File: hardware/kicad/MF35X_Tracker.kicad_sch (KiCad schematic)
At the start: 14 parts, among them J1 External GPIO11 logic output, J2 5V power input from DC/DC, J3 VDO oil-temp NTC - return/cas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, J4 Oil-pressure sender - return/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, J5 Vehicle battery sense input, U1 Freenove ESP32-S3 WROOM Lite 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, U2 ADS1115 @ 0x48, U3 GPS module - VCC TBD, U4 MAX31855 K-type - VCC TBD, U5 HY-M154 / PC817 RPM interface

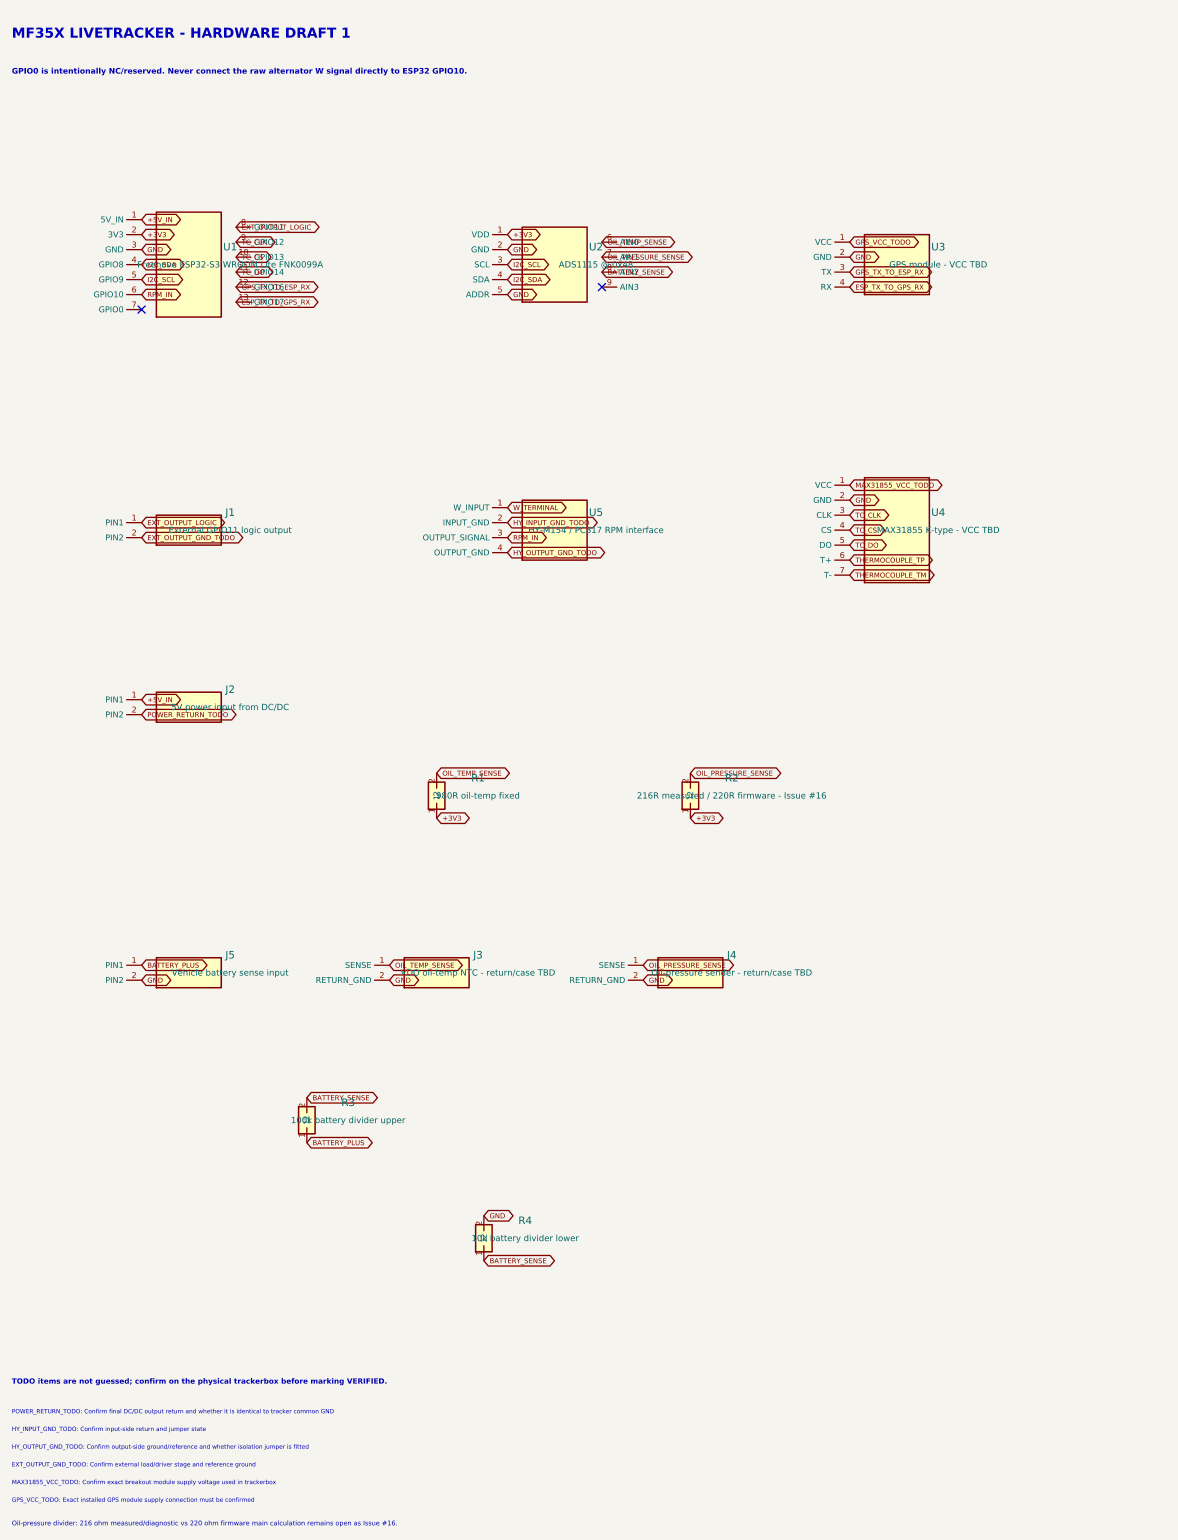
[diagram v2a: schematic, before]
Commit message: Regenerate confirmed trackerbox wiring
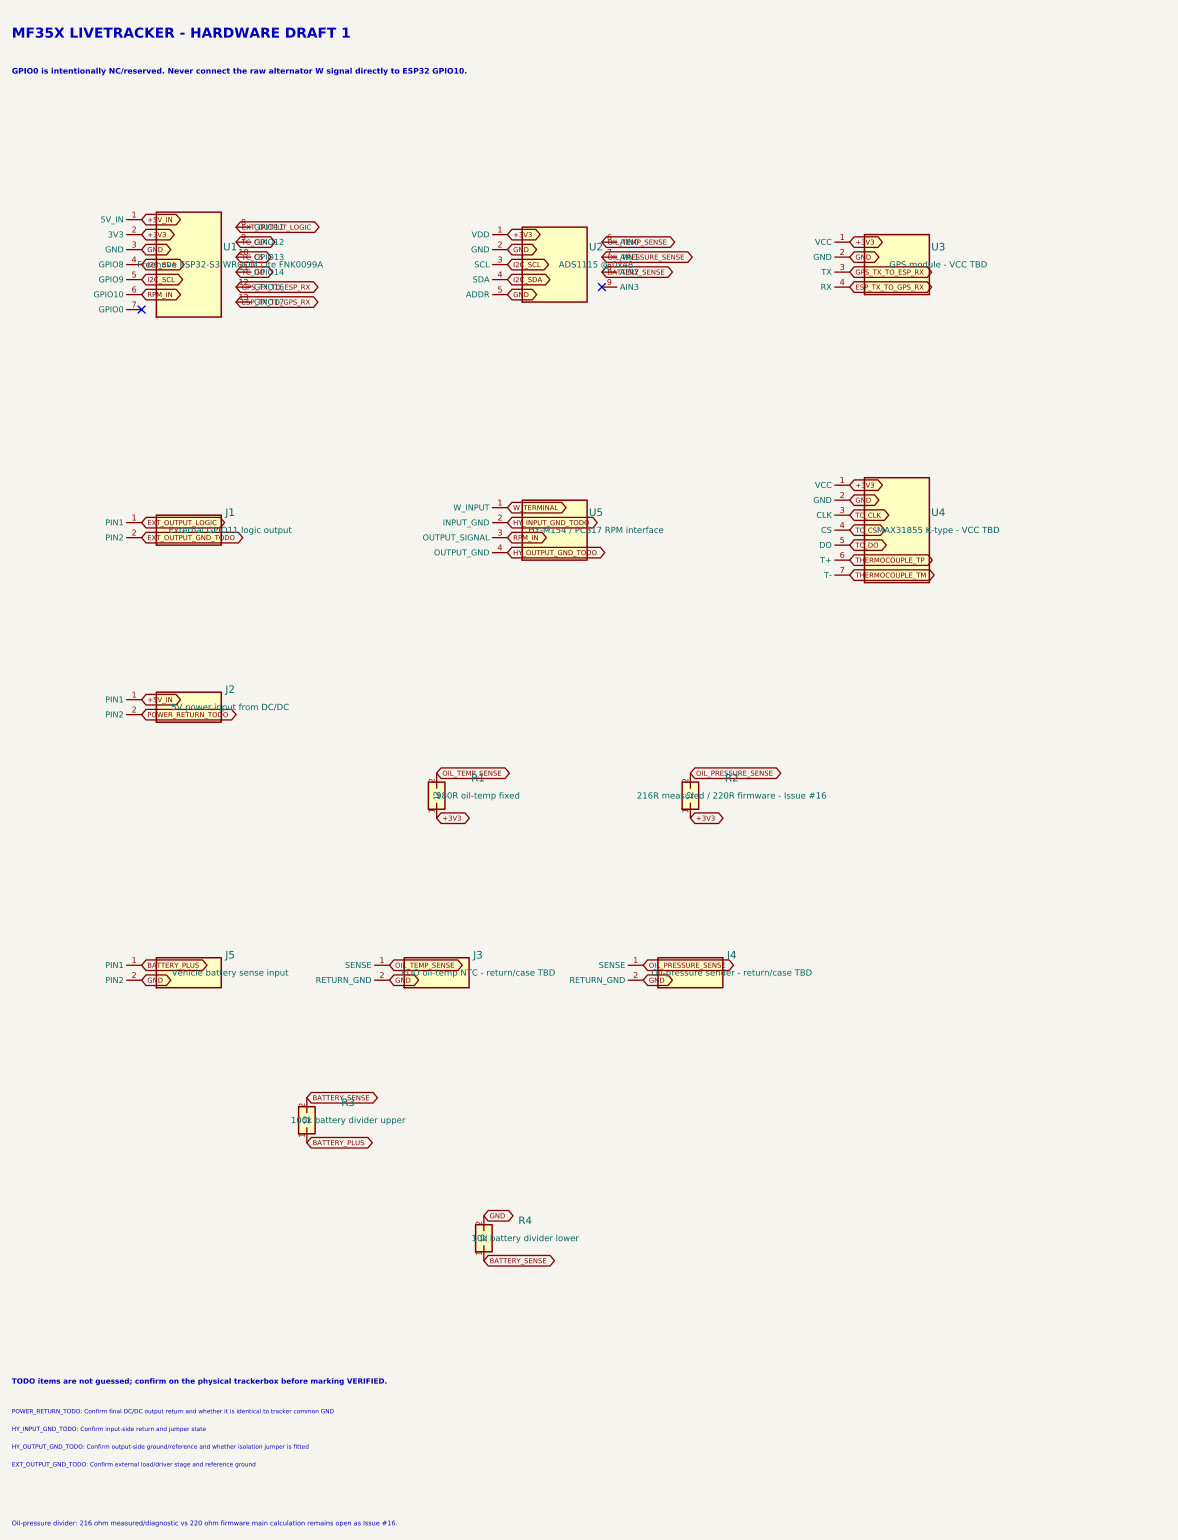
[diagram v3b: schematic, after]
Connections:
- net GPS_VCC_TODO is gone; now on net +3V3: U3.1 (VCC)
- net MAX31855_VCC_TODO is gone; now on net +3V3: U4.1 (VCC)
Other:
- note removed: "GPS_VCC_TODO: Exact installed GPS module supply connection must be confirmed"
- note removed: "MAX31855_VCC_TODO: Confirm exact breakout module supply voltage used in trackerbox"
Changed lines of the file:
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@@
     (effects (font (size 0.85 0.85)) (justify left))
   )
-  (global_label "GPS_VCC_TODO" (shape bidirectional) (at 162.00 51.19 0)
+  (global_label "+3V3" (shape bidirectional) (at 162.00 51.19 0)
     (effects (font (size 0.85 0.85)) (justify left))
   )
@@
     (effects (font (size 0.85 0.85)) (justify left))
   )
-  (global_label "MAX31855_VCC_TODO" (shape bidirectional) (at 162.00 92.38 0)
+  (global_label "+3V3" (shape bidirectional) (at 162.00 92.38 0)
     (effects (font (size 0.85 0.85)) (justify left))
   )
@@
     (effects (font (size 0.72 0.72)) (justify left bottom))
   )
-  (text "MAX31855_VCC_TODO: Confirm exact breakout module supply voltage used in trackerbox" (at 20.00 262.00 0)
-    (effects (font (size 0.72 0.72)) (justify left bottom))
-  )
-  (text "GPS_VCC_TODO: Exact installed GPS module supply connection must be confirmed" (at 20.00 265.00 0)
-    (effects (font (size 0.72 0.72)) (justify left bottom))
-  )

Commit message: Regenerate HY-M154 and solenoid wiring
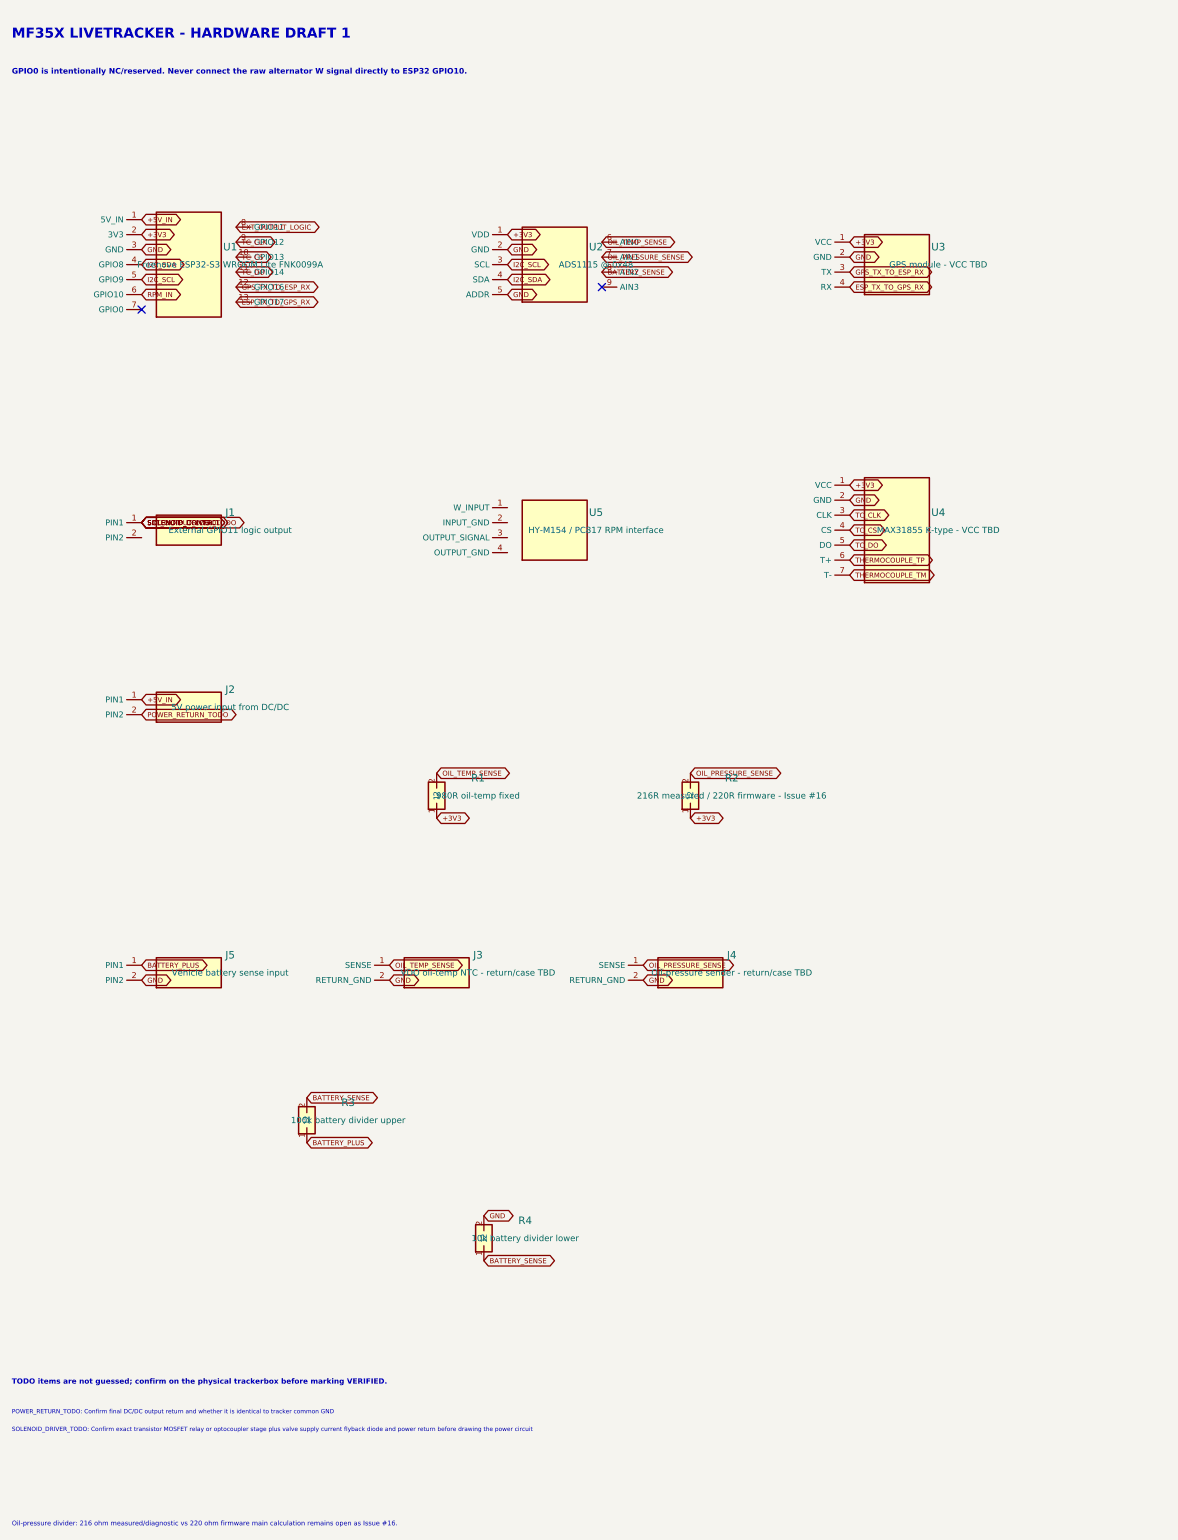
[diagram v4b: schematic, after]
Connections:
- net RPM_IN: no longer U5.3 (OUTPUT_SIGNAL)
- net EXT_OUTPUT_GND_TODO: no longer names the net of J1.2 (PIN2)
- net HY_INPUT_GND_TODO: no longer names the net of U5.2 (INPUT_GND)
- net HY_OUTPUT_GND_TODO: no longer names the net of U5.4 (OUTPUT_GND)
- net W_TERMINAL: no longer names the net of U5.1 (W_INPUT)
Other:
- note added: "SOLENOID_DRIVER_TODO: Confirm exact transistor MOSFET relay or optocoupler stage plus valve supply current flyback diode and power return before drawing the power circuit"
- note removed: "EXT_OUTPUT_GND_TODO: Confirm external load/driver stage and reference ground"
- note removed: "HY_INPUT_GND_TODO: Confirm input-side return and jumper state"
- note removed: "HY_OUTPUT_GND_TODO: Confirm output-side ground/reference and whether isolation jumper is fitted"
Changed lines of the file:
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@@
     (effects (font (size 0.85 0.85)) (justify left))
   )
-  (global_label "EXT_OUTPUT_GND_TODO" (shape bidirectional) (at 42.00 101.27 0)
+  (global_label "SOLENOID_CONTROL" (shape bidirectional) (at 42.00 98.73 0)
+    (effects (font (size 0.85 0.85)) (justify left))
+  )
+  (global_label "SOLENOID_DRIVER_TODO" (shape bidirectional) (at 42.00 98.73 0)
     (effects (font (size 0.85 0.85)) (justify left))
   )
@@
     (effects (font (size 0.85 0.85)) (justify left))
   )
-  (global_label "HY_INPUT_GND_TODO" (shape bidirectional) (at 104.00 98.73 0)
-    (effects (font (size 0.85 0.85)) (justify left))
-  )
-  (global_label "HY_OUTPUT_GND_TODO" (shape bidirectional) (at 104.00 103.81 0)
-    (effects (font (size 0.85 0.85)) (justify left))
-  )
-  (global_label "RPM_IN" (shape bidirectional) (at 104.00 101.27 0)
-    (effects (font (size 0.85 0.85)) (justify left))
-  )
-  (global_label "W_TERMINAL" (shape bidirectional) (at 104.00 96.19 0)
-    (effects (font (size 0.85 0.85)) (justify left))
-  )
   (no_connect (at 42.00 62.62))
   (no_connect (at 120.00 58.81))
@@
     (effects (font (size 0.72 0.72)) (justify left bottom))
   )
-  (text "HY_INPUT_GND_TODO: Confirm input-side return and jumper state" (at 20.00 253.00 0)
+  (text "SOLENOID_DRIVER_TODO: Confirm exact transistor MOSFET relay or optocoupler stage plus valve supply current flyback diode and power return before drawing the power circuit" (at 20.00 253.00 0)
     (effects (font (size 0.72 0.72)) (justify left bottom))
   )
-  (text "HY_OUTPUT_GND_TODO: Confirm output-side ground/reference and whether isolation jumper is fitted" (at 20.00 256.00 0)
-    (effects (font (size 0.72 0.72)) (justify left bottom))
-  )
-  (text "EXT_OUTPUT_GND_TODO: Confirm external load/driver stage and reference ground" (at 20.00 259.00 0)
-    (effects (font (size 0.72 0.72)) (justify left bottom))
-  )

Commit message: Generate KiCad trackerbox HW-REV1
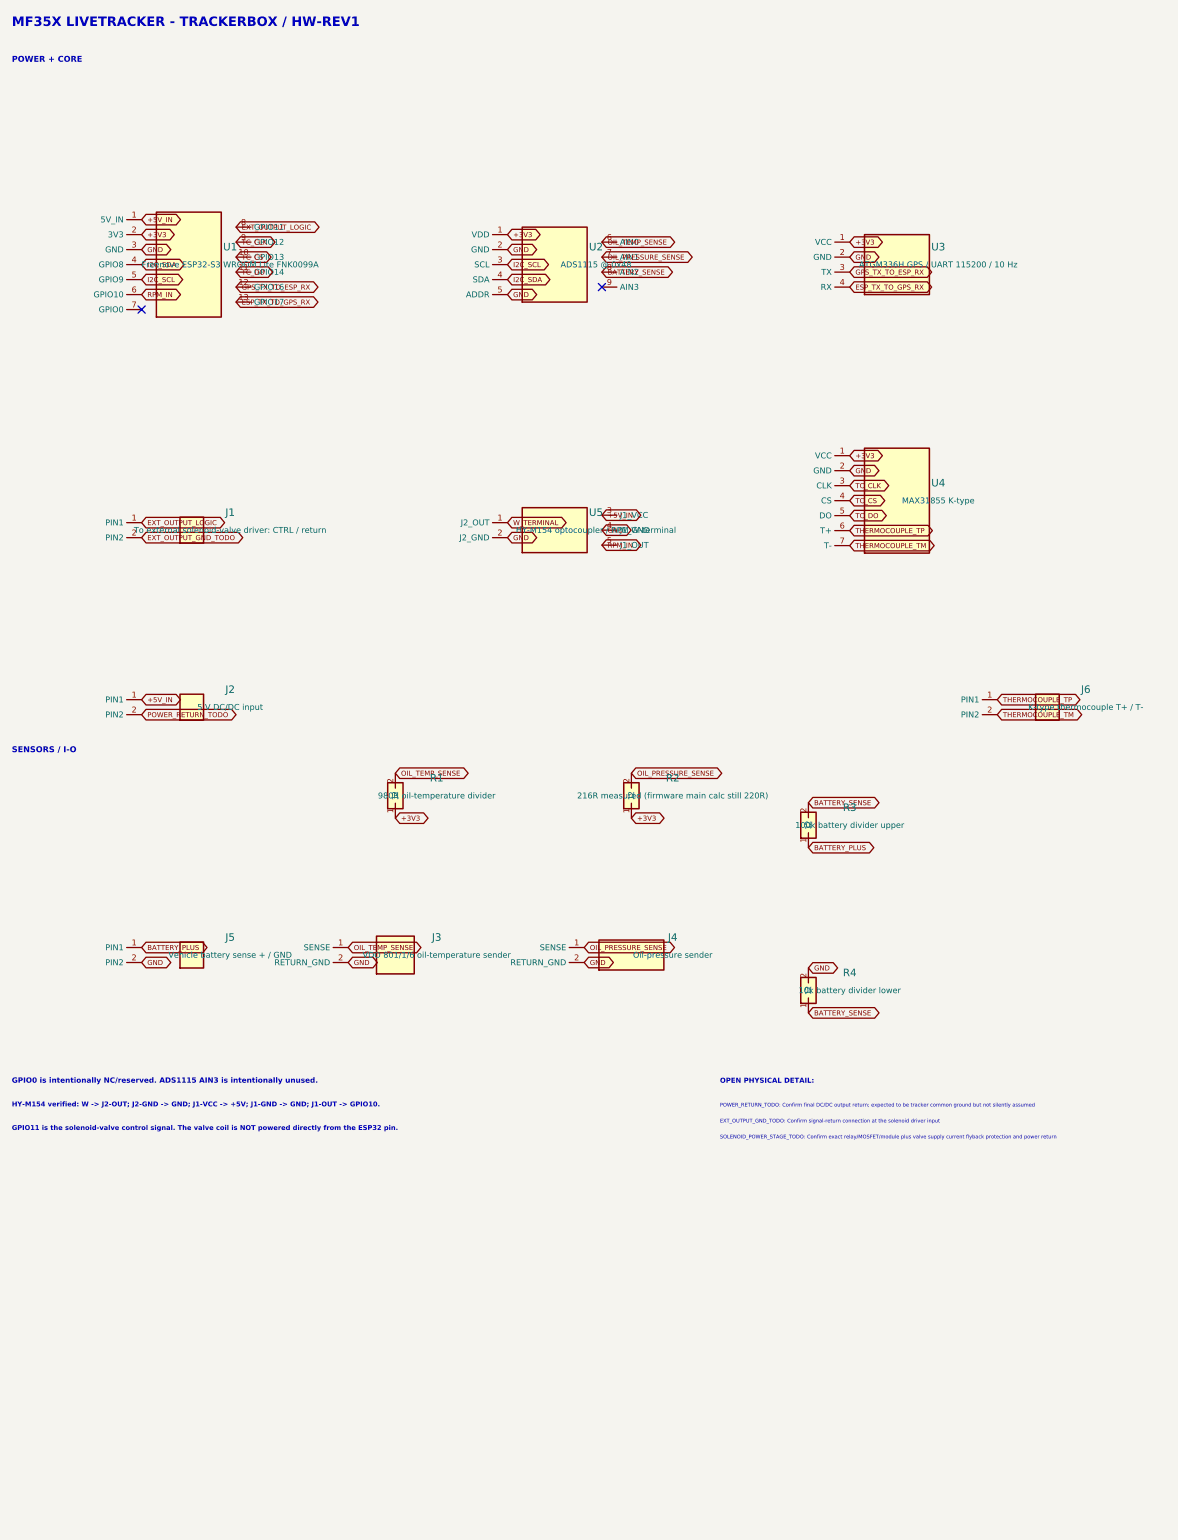
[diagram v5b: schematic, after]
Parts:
- added J6: K-type thermocouple T+ / T-, symbol Connector_Generic:Conn_01x02
- J1: value External GPIO11 logic output -> To external solenoid-valve driver: CTRL / return; symbol MF35X:CONN2 -> Connector_Generic:Conn_01x02
- J2: value 5V power input from DC/DC -> 5 V DC/DC input; symbol MF35X:CONN2 -> Connector_Generic:Conn_01x02
- J3: value VDO oil-temp NTC - return/case TBD -> VDO 801/1/6 oil-temperature sender; symbol MF35X:SENSOR2 -> MF35X:SENSOR_CASE
- J4: value Oil-pressure sender - return/case TBD -> Oil-pressure sender
- J5: value Vehicle battery sense input -> Vehicle battery sense + / GND; symbol MF35X:CONN2 -> Connector_Generic:Conn_01x02
- R1: value 980R oil-temp fixed -> 980R oil-temperature divider; symbol MF35X:R -> Device:R
- R2: value 216R measured / 220R firmware - Issue #16 -> 216R measured (firmware main calc still 220R); symbol MF35X:R -> Device:R
- R3, R4: symbol MF35X:R -> Device:R
- U3: value GPS module - VCC TBD -> ATGM336H GPS / UART 115200 / 10 Hz; symbol MF35X:GPS -> MF35X:GPS_ATGM336H
- U4: value MAX31855 K-type - VCC TBD -> MAX31855 K-type
- U5: value HY-M154 / PC817 RPM interface -> HY-M154 optocoupler / RPM W-terminal
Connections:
- net +5V_IN: now also U5.3 (J1_VCC)
- net GND: now also U5.2 (J2_GND), U5.4 (J1_GND)
- net RPM_IN: now also U5.5 (J1_OUT)
- net THERMOCOUPLE_TM: now also J6.2 (PIN2)
- net THERMOCOUPLE_TP: now also J6.1 (PIN1)
- net EXT_OUTPUT_GND_TODO: now reaches J1.2 (PIN2)
- net W_TERMINAL: now reaches U5.1 (J2_OUT)
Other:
- note added: "EXT_OUTPUT_GND_TODO: Confirm signal-return connection at the solenoid driver input"
- note added: "GPIO0 is intentionally NC/reserved. ADS1115 AIN3 is intentionally unused."
- note added: "GPIO11 is the solenoid-valve control signal. The valve coil is NOT powered directly from the ESP32 pin."
- note added: "HY-M154 verified: W -> J2-OUT; J2-GND -> GND; J1-VCC -> +5V; J1-GND -> GND; J1-OUT -> GPIO10."
- note added: "MF35X LIVETRACKER - TRACKERBOX / HW-REV1"
- note added: "OPEN PHYSICAL DETAIL:"
- note added: "POWER + CORE"
- note added: "POWER_RETURN_TODO: Confirm final DC/DC output return; expected to be tracker common ground but not silently assumed"
- note added: "SENSORS / I-O"
- note added: "SOLENOID_POWER_STAGE_TODO: Confirm exact relay/MOSFET/module plus valve supply current flyback protection and power return"
- note removed: "GPIO0 is intentionally NC/reserved. Never connect the raw alternator W signal directly to ESP32 GPIO10."
- note removed: "MF35X LIVETRACKER - HARDWARE DRAFT 1"
- note removed: "Oil-pressure divider: 216 ohm measured/diagnostic vs 220 ohm firmware main calculation remains open as Issue #16."
- note removed: "POWER_RETURN_TODO: Confirm final DC/DC output return and whether it is identical to tracker common GND"
- note removed: "SOLENOID_DRIVER_TODO: Confirm exact transistor MOSFET relay or optocoupler stage plus valve supply current flyback diode and power return before drawing the power circuit"
- note removed: "TODO items are not guessed; confirm on the physical trackerbox before marking VERIFIED."
- title: MF35X Livetracker - Trackerbox Wiring -> MF35X Livetracker - Trackerbox Electrical Schematic
- moved on the sheet: J1, J2, J3, J4, J5, R1, R2, R3, R4, U4
